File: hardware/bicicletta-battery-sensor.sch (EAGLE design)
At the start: 17 parts, among them IC1 LMV324MZ

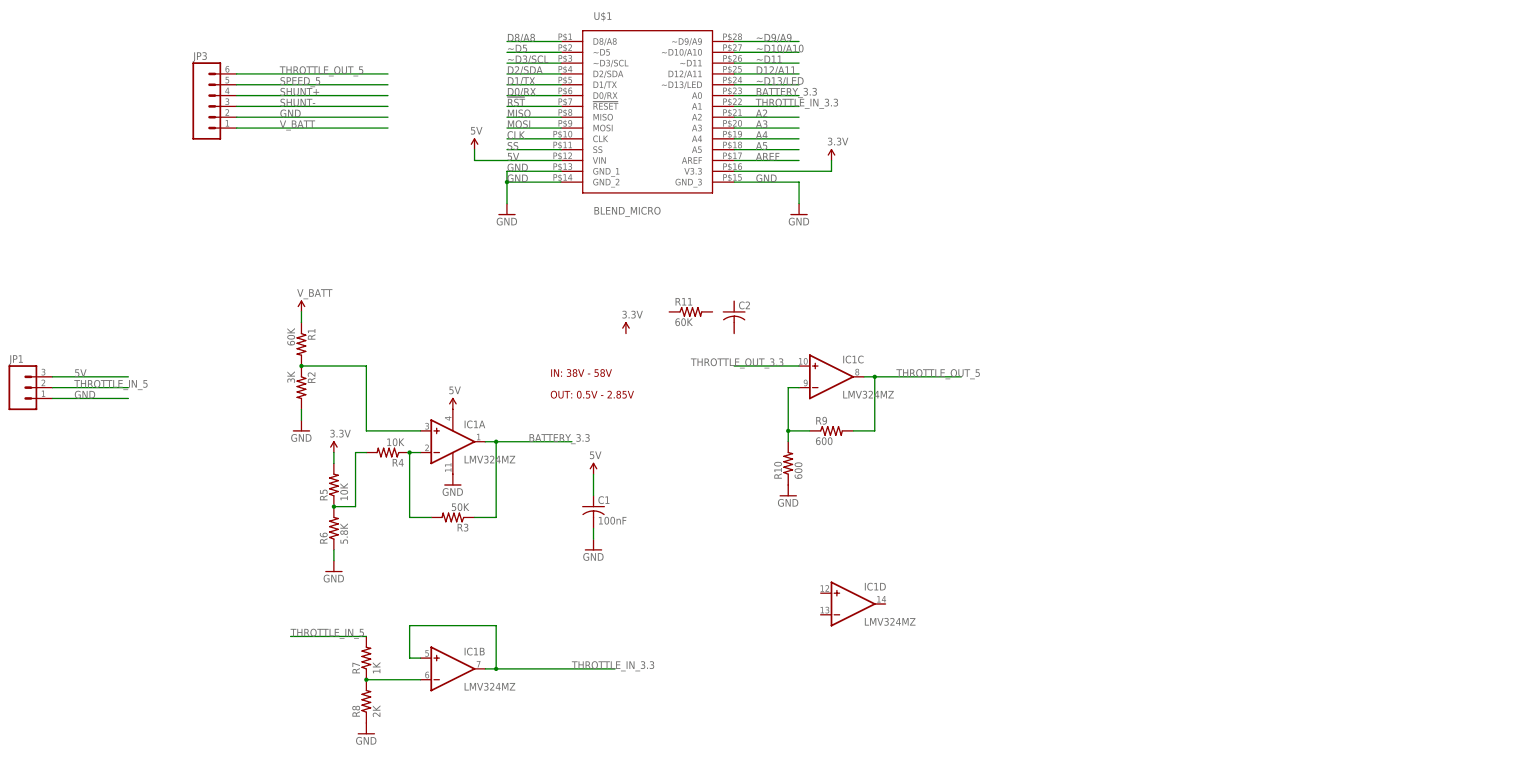
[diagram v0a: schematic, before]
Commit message: Let's use the LMP92064!
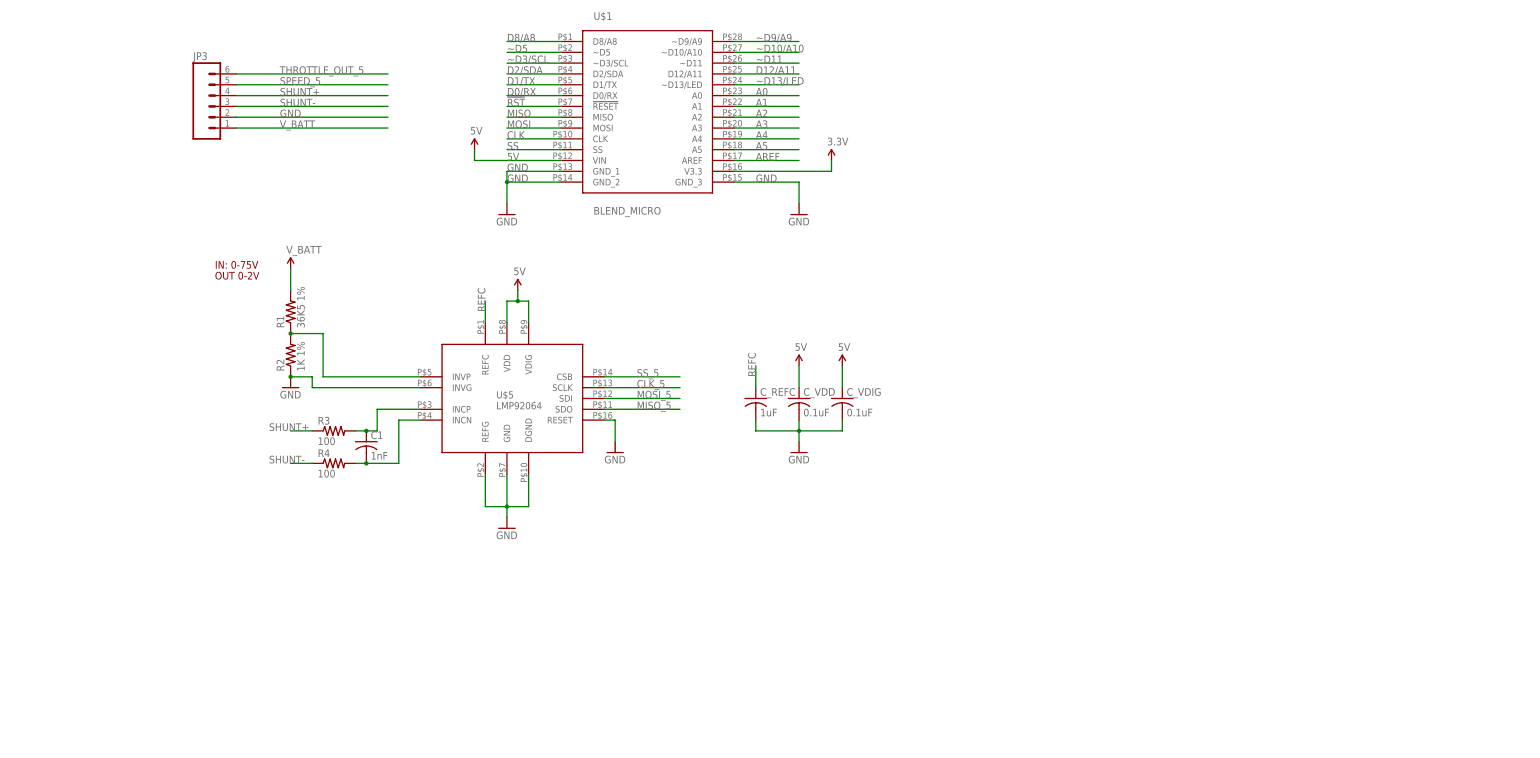
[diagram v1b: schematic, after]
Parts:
- removed C2: (no value), rcl:C-USC0603
- removed IC1: LMV324MZ, linear:LMV324MZ
- removed JP1: (no value), SparkFun-Connectors:M03PTH
- removed R10, R9: 600, rcl:R-US_R0603
- removed R11: 60K, rcl:R-US_R0603
- removed R5: 10K, rcl:R-US_R0603
- removed R6: 5.8K, rcl:R-US_R0603
- removed R7: 1K, rcl:R-US_R0603
- removed R8: 2K, rcl:R-US_R0603
- added C_REFC: 1uF, rcl:C-USC0603
- added C_VDD, C_VDIG: 0.1uF, rcl:C-USC0603
- added U$5: LMP92064, Railstars:LMP92064
- C1: value 100nF -> 1nF
- R1: value 60K -> 36K5 1%
- R2: value 3K -> 1K 1%
- R3: value 50K -> 100
- R4: value 10K -> 100
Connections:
- removed net BATTERY_3.3: IC1A.OUT, R3.1, U$1.A0
- removed net BIAS: R4.2, R5.1, R6.2
- removed net N$11: IC1B.-IN, R7.1, R8.2
- removed net THROTTLE_IN_3.3: IC1B.+IN, IC1B.OUT, U$1.A1
- removed net THROTTLE_IN_5: JP1.2, R7.2
- removed net THROTTLE_OUT_3.3: IC1C.+IN
- new net A0: U$1.A0
- new net A1: U$1.A1
- new net CLK_5: U$5.SCLK
- new net MISO_5: U$5.SDO
- new net MOSI_5: U$5.SDI
- new net N$4: C1.2, R4.2, U$5.INCN
- new net REFC: C_REFC.1, U$5.REFC
- new net SS_5: U$5.CSB
- net 3.3V: no longer R5.2
- net 5V: now also C_VDD.1, C_VDIG.1, U$5.VDD, U$5.VDIG; no longer C1.1, IC1P.V+, JP1.3
- net GND: now also R2.1, U$5.DGND, U$5.GND, U$5.INVG, U$5.REFG, U$5.RESET; no longer C1.2, IC1P.V-, JP1.1, R10.1, R2.2, R6.1, R8.1
- net N$1: now also R1.1, R2.2, U$5.INVP; no longer IC1C.-IN, R10.2, R9.1
- net N$2: now also C_REFC.2, C_VDD.2, C_VDIG.2; no longer IC1A.+IN, R1.2, R2.1
- net N$3: now also C1.1, U$5.INCP; no longer IC1A.-IN, R4.1
- net SHUNT+: now also R3.1
- net SHUNT-: now also R4.1
- net THROTTLE_OUT_5: no longer IC1C.OUT, R9.2
- net V_BATT: now also R1.2; no longer R1.1
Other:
- note added: "IN: 0-75V"
- note added: "OUT 0-2V"
- note removed: "IN: 38V - 58V"
- note removed: "OUT: 0.5V - 2.85V"
- moved on the sheet: C1, R1, R2, R3, R4

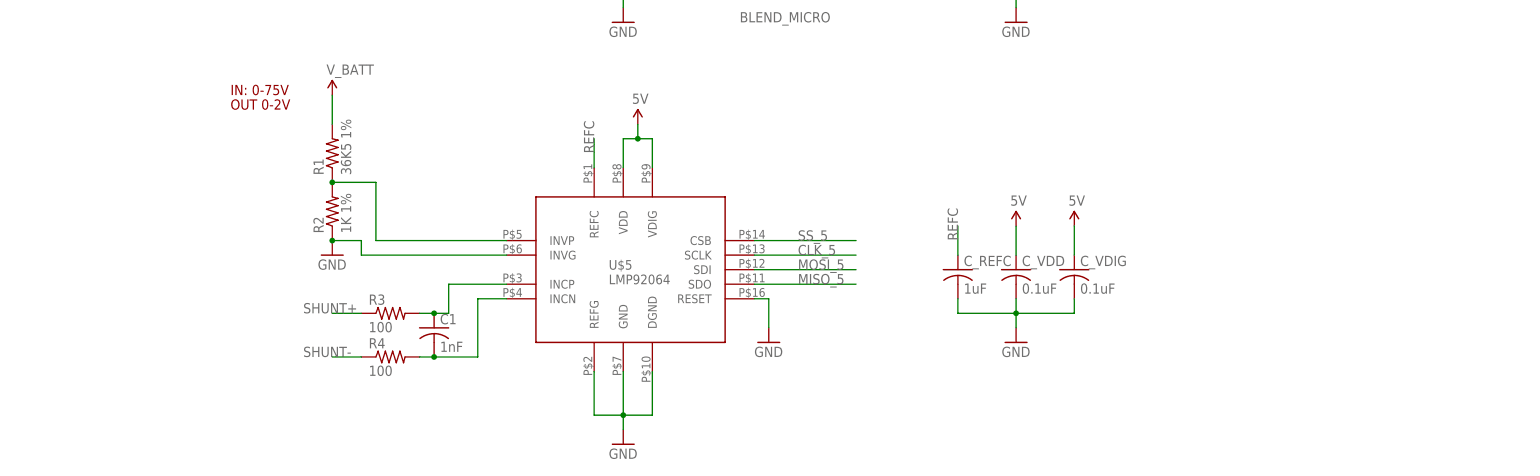
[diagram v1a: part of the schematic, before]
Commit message: Add level shifter
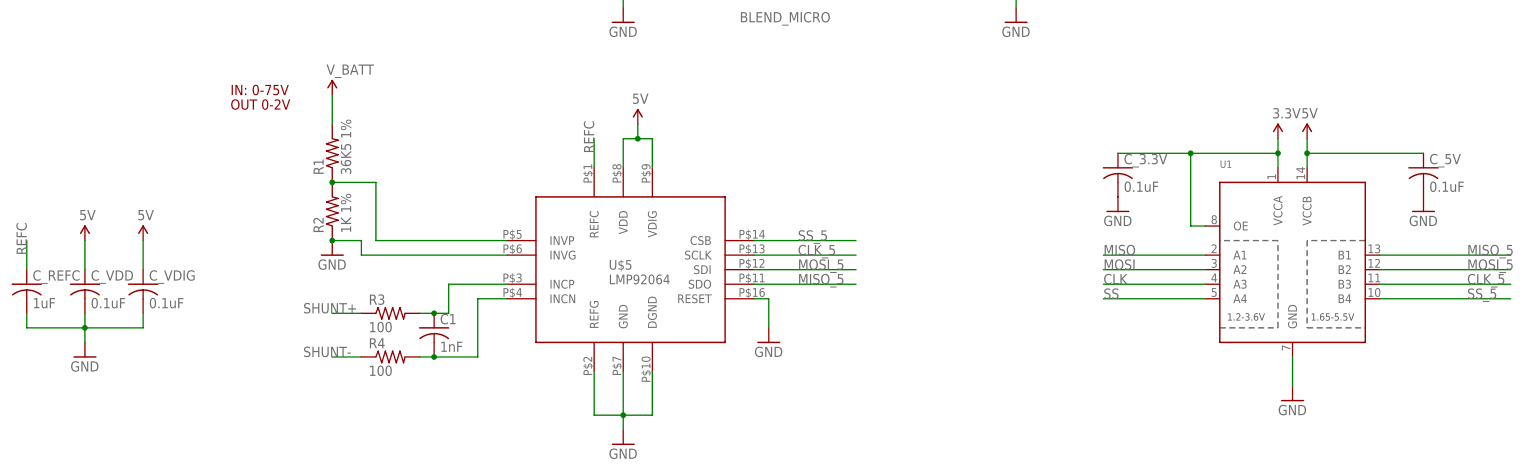
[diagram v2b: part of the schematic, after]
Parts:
- added C_3.3V, C_5V: 0.1uF, rcl:C-USC0603
- added U1: (no value), adafruit:TXB0104PWR
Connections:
- removed net N$2: C_REFC.2, C_VDD.2, C_VDIG.2
- net 3.3V: now also C_3.3V.1, U1.OE, U1.VCCA
- net 5V: now also C_5V.1, U1.VCCB
- net CLK: now also U1.A3
- net CLK_5: now also U1.B3
- net GND: now also C_3.3V.2, C_5V.2, C_REFC.2, C_VDD.2, C_VDIG.2, U1.GND
- net MISO: now also U1.A1
- net MISO_5: now also U1.B1
- net MOSI: now also U1.A2
- net MOSI_5: now also U1.B2
- net SS: now also U1.A4
- net SS_5: now also U1.B4
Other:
- moved on the sheet: C_REFC, C_VDD, C_VDIG
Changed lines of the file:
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@@
 <part name="R4" library="rcl" deviceset="R-US_" device="R0603" value="100"/>
 <part name="C1" library="rcl" deviceset="C-US" device="C0603" value="1nF"/>
+<part name="U1" library="adafruit" deviceset="TXB0104PWR" device=""/>
+<part name="GND7" library="SparkFun-Aesthetics" deviceset="GND" device=""/>
+<part name="P+2" library="SparkFun-Aesthetics" deviceset="3.3V" device=""/>
+<part name="U$9" library="SparkFun-Aesthetics" deviceset="5V" device=""/>
+<part name="C_3.3V" library="rcl" deviceset="C-US" device="C0603" value="0.1uF"/>
+<part name="C_5V" library="rcl" deviceset="C-US" device="C0603" value="0.1uF"/>
+<part name="GND8" library="SparkFun-Aesthetics" deviceset="GND" device=""/>
+<part name="GND9" library="SparkFun-Aesthetics" deviceset="GND" device=""/>
 </parts>
 <sheets>
@@
 <instance part="U$5" gate="G$1" x="106.68" y="129.54"/>
 <instance part="GND1" gate="1" x="134.62" y="116.84"/>
-<instance part="C_REFC" gate="G$1" x="167.64" y="129.54"/>
-<instance part="GND6" gate="1" x="177.8" y="116.84"/>
-<instance part="C_VDD" gate="G$1" x="177.8" y="129.54"/>
-<instance part="C_VDIG" gate="G$1" x="187.96" y="129.54"/>
-<instance part="U$6" gate="G$1" x="177.8" y="137.16"/>
-<instance part="U$8" gate="G$1" x="187.96" y="137.16"/>
+<instance part="C_REFC" gate="G$1" x="5.08" y="127"/>
+<instance part="GND6" gate="1" x="15.24" y="114.3"/>
+<instance part="C_VDD" gate="G$1" x="15.24" y="127"/>
+<instance part="C_VDIG" gate="G$1" x="25.4" y="127"/>
+<instance part="U$6" gate="G$1" x="15.24" y="134.62"/>
+<instance part="U$8" gate="G$1" x="25.4" y="134.62"/>
 <instance part="R3" gate="G$1" x="68.58" y="121.92"/>
 <instance part="R4" gate="G$1" x="68.58" y="114.3"/>
 <instance part="C1" gate="G$1" x="76.2" y="119.38"/>
+<instance part="U1" gate="G$1" x="226.06" y="129.54"/>
+<instance part="GND7" gate="1" x="226.06" y="106.68"/>
+<instance part="P+2" gate="G$1" x="223.52" y="152.4"/>
+<instance part="U$9" gate="G$1" x="228.6" y="152.4"/>
+<instance part="C_3.3V" gate="G$1" x="195.58" y="147.32"/>
+<instance part="C_5V" gate="G$1" x="248.92" y="147.32"/>
+<instance part="GND8" gate="1" x="248.92" y="139.7"/>
+<instance part="GND9" gate="1" x="195.58" y="139.7"/>
 </instances>
 <busses>
@@
 <pinref part="U$1" gate="G$1" pin="MISO"/>
 </segment>
+<segment>
+<pinref part="U1" gate="G$1" pin="A1"/>
+<wire x1="210.82" y1="132.08" x2="193.04" y2="132.08" width="0.1524" layer="91"/>
+<label x="193.04" y="132.08" size="1.778" layer="95"/>
+</segment>
 </net>
 <net name="MOSI" class="0">
@@
 <pinref part="U$1" gate="G$1" pin="MOSI"/>
 </segment>
+<segment>
+<pinref part="U1" gate="G$1" pin="A2"/>
+<wire x1="210.82" y1="129.54" x2="193.04" y2="129.54" width="0.1524" layer="91"/>
+<label x="193.04" y="129.54" size="1.778" layer="95"/>
+</segment>
 </net>
 <net name="CLK" class="0">
@@
 <pinref part="U$1" gate="G$1" pin="CLK"/>
 </segment>
+<segment>
+<pinref part="U1" gate="G$1" pin="A3"/>
+<wire x1="210.82" y1="127" x2="193.04" y2="127" width="0.1524" layer="91"/>
+<label x="193.04" y="127" size="1.778" layer="95"/>
+</segment>
 </net>
 <net name="SS" class="0">
@@
 <label x="109.22" y="187.96" size="1.778" layer="95"/>
 <pinref part="U$1" gate="G$1" pin="SS"/>
+</segment>
+<segment>
+<pinref part="U1" gate="G$1" pin="A4"/>
+<wire x1="210.82" y1="124.46" x2="193.04" y2="124.46" width="0.1524" layer="91"/>
+<label x="193.04" y="124.46" size="1.778" layer="95"/>
 </segment>
 </net>
@@
 <junction x="109.22" y="104.14"/>
 </segment>
+<segment>
+<pinref part="C_VDIG" gate="G$1" pin="2"/>
+<wire x1="25.4" y1="121.92" x2="25.4" y2="119.38" width="0.1524" layer="91"/>
+<wire x1="25.4" y1="119.38" x2="15.24" y2="119.38" width="0.1524" layer="91"/>
+<wire x1="15.24" y1="119.38" x2="15.24" y2="116.84" width="0.1524" layer="91"/>
+<pinref part="C_REFC" gate="G$1" pin="2"/>
+<wire x1="5.08" y1="121.92" x2="5.08" y2="119.38" width="0.1524" layer="91"/>
+<wire x1="5.08" y1="119.38" x2="15.24" y2="119.38" width="0.1524" layer="91"/>
+<pinref part="C_VDD" gate="G$1" pin="2"/>
+<wire x1="15.24" y1="121.92" x2="15.24" y2="119.38" width="0.1524" layer="91"/>
+<junction x="15.24" y="119.38"/>
+<pinref part="GND6" gate="1" pin="GND"/>
+</segment>
+<segment>
+<pinref part="U1" gate="G$1" pin="GND"/>
+<wire x1="226.06" y1="114.3" x2="226.06" y2="109.22" width="0.1524" layer="91"/>
+<pinref part="GND7" gate="1" pin="GND"/>
+</segment>
+<segment>
+<pinref part="C_5V" gate="G$1" pin="2"/>
+<pinref part="GND8" gate="1" pin="GND"/>
+</segment>
+<segment>
+<pinref part="C_3.3V" gate="G$1" pin="2"/>
+<pinref part="GND9" gate="1" pin="GND"/>
+</segment>
 </net>
 <net name="~D9/A9" class="0">
@@
 <pinref part="C_VDD" gate="G$1" pin="1"/>
 <pinref part="U$6" gate="G$1" pin="5V"/>
-<wire x1="177.8" y1="137.16" x2="177.8" y2="132.08" width="0.1524" layer="91"/>
+<wire x1="15.24" y1="134.62" x2="15.24" y2="129.54" width="0.1524" layer="91"/>
 </segment>
 <segment>
 <pinref part="U$8" gate="G$1" pin="5V"/>
 <pinref part="C_VDIG" gate="G$1" pin="1"/>
-<wire x1="187.96" y1="137.16" x2="187.96" y2="132.08" width="0.1524" layer="91"/>
+<wire x1="25.4" y1="134.62" x2="25.4" y2="129.54" width="0.1524" layer="91"/>
+</segment>
+<segment>
+<pinref part="U1" gate="G$1" pin="VCCB"/>
+<wire x1="228.6" y1="147.32" x2="228.6" y2="149.86" width="0.1524" layer="91"/>
+<pinref part="U$9" gate="G$1" pin="5V"/>
+<pinref part="C_5V" gate="G$1" pin="1"/>
+<wire x1="228.6" y1="149.86" x2="228.6" y2="152.4" width="0.1524" layer="91"/>
+<wire x1="228.6" y1="149.86" x2="248.92" y2="149.86" width="0.1524" layer="91"/>
+<junction x="228.6" y="149.86"/>
 </segment>
 </net>
@@
 <wire x1="162.56" y1="182.88" x2="185.42" y2="182.88" width="0.1524" layer="91"/>
 <wire x1="185.42" y1="182.88" x2="185.42" y2="185.42" width="0.1524" layer="91"/>
+</segment>
+<segment>
+<pinref part="U1" gate="G$1" pin="VCCA"/>
+<wire x1="223.52" y1="147.32" x2="223.52" y2="149.86" width="0.1524" layer="91"/>
+<pinref part="P+2" gate="G$1" pin="3.3V"/>
+<pinref part="U1" gate="G$1" pin="OE"/>
+<wire x1="223.52" y1="149.86" x2="223.52" y2="152.4" width="0.1524" layer="91"/>
+<wire x1="210.82" y1="137.16" x2="208.28" y2="137.16" width="0.1524" layer="91"/>
+<wire x1="208.28" y1="137.16" x2="208.28" y2="149.86" width="0.1524" layer="91"/>
+<wire x1="208.28" y1="149.86" x2="223.52" y2="149.86" width="0.1524" layer="91"/>
+<pinref part="C_3.3V" gate="G$1" pin="1"/>
+<wire x1="208.28" y1="149.86" x2="195.58" y2="149.86" width="0.1524" layer="91"/>
+<junction x="223.52" y="149.86"/>
+<junction x="208.28" y="149.86"/>
 </segment>
 </net>
@@
 <segment>
 <pinref part="C_REFC" gate="G$1" pin="1"/>
-<wire x1="167.64" y1="132.08" x2="167.64" y2="137.16" width="0.1524" layer="91"/>
-<label x="167.64" y="134.62" size="1.778" layer="95" rot="R90"/>
-</segment>
-</net>
-<net name="N$2" class="0">
-<segment>
-<pinref part="C_VDIG" gate="G$1" pin="2"/>
-<wire x1="187.96" y1="124.46" x2="187.96" y2="121.92" width="0.1524" layer="91"/>
-<wire x1="187.96" y1="121.92" x2="177.8" y2="121.92" width="0.1524" layer="91"/>
-<wire x1="177.8" y1="121.92" x2="177.8" y2="119.38" width="0.1524" layer="91"/>
-<pinref part="C_REFC" gate="G$1" pin="2"/>
-<wire x1="167.64" y1="124.46" x2="167.64" y2="121.92" width="0.1524" layer="91"/>
-<wire x1="167.64" y1="121.92" x2="177.8" y2="121.92" width="0.1524" layer="91"/>
-<pinref part="C_VDD" gate="G$1" pin="2"/>
-<wire x1="177.8" y1="124.46" x2="177.8" y2="121.92" width="0.1524" layer="91"/>
-<junction x="177.8" y="121.92"/>
+<wire x1="5.08" y1="129.54" x2="5.08" y2="134.62" width="0.1524" layer="91"/>
+<label x="5.08" y="132.08" size="1.778" layer="95" rot="R90"/>
 </segment>
 </net>
@@
 <label x="139.7" y="134.62" size="1.778" layer="95"/>
 </segment>
+<segment>
+<pinref part="U1" gate="G$1" pin="B4"/>
+<wire x1="241.3" y1="124.46" x2="264.16" y2="124.46" width="0.1524" layer="91"/>
+<label x="256.54" y="124.46" size="1.778" layer="95"/>
+</segment>
 </net>
 <net name="CLK_5" class="0">
@@
 <label x="139.7" y="132.08" size="1.778" layer="95"/>
 </segment>
+<segment>
+<pinref part="U1" gate="G$1" pin="B3"/>
+<wire x1="241.3" y1="127" x2="264.16" y2="127" width="0.1524" layer="91"/>
+<label x="256.54" y="127" size="1.778" layer="95"/>
+</segment>
 </net>
 <net name="MOSI_5" class="0">
@@
 <label x="139.7" y="129.54" size="1.778" layer="95"/>
 </segment>
+<segment>
+<pinref part="U1" gate="G$1" pin="B2"/>
+<wire x1="241.3" y1="129.54" x2="264.16" y2="129.54" width="0.1524" layer="91"/>
+<label x="256.54" y="129.54" size="1.778" layer="95"/>
+</segment>
 </net>
 <net name="MISO_5" class="0">
@@
 <label x="139.7" y="127" size="1.778" layer="95"/>
 </segment>
-</net>
+<segment>
+<pinref part="U1" gate="G$1" pin="B1"/>
+<wire x1="241.3" y1="132.08" x2="264.16" y2="132.08" width="0.1524" layer="91"/>
+<label x="256.54" y="132.08" size="1.778" layer="95"/>
+</segment>
+</net>
